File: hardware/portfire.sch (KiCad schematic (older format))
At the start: 32 parts, among them IC4 25AA02E48, IC5 STM32F4xxVxTx, P1 1, P10 10, P11 11, P12 12, P13 13, P14 14, P15 15, P16 16, P17 17, P18 18, P19 19, P2 2, P20 20, P21 21, P22 22, P23 23, P24 24, P25 25, P26 26, P27 27, P28 28, P29 29, P3 3, P30 30, P4 4, P5 5, P6 6, P7 7, P8 8, P9 9

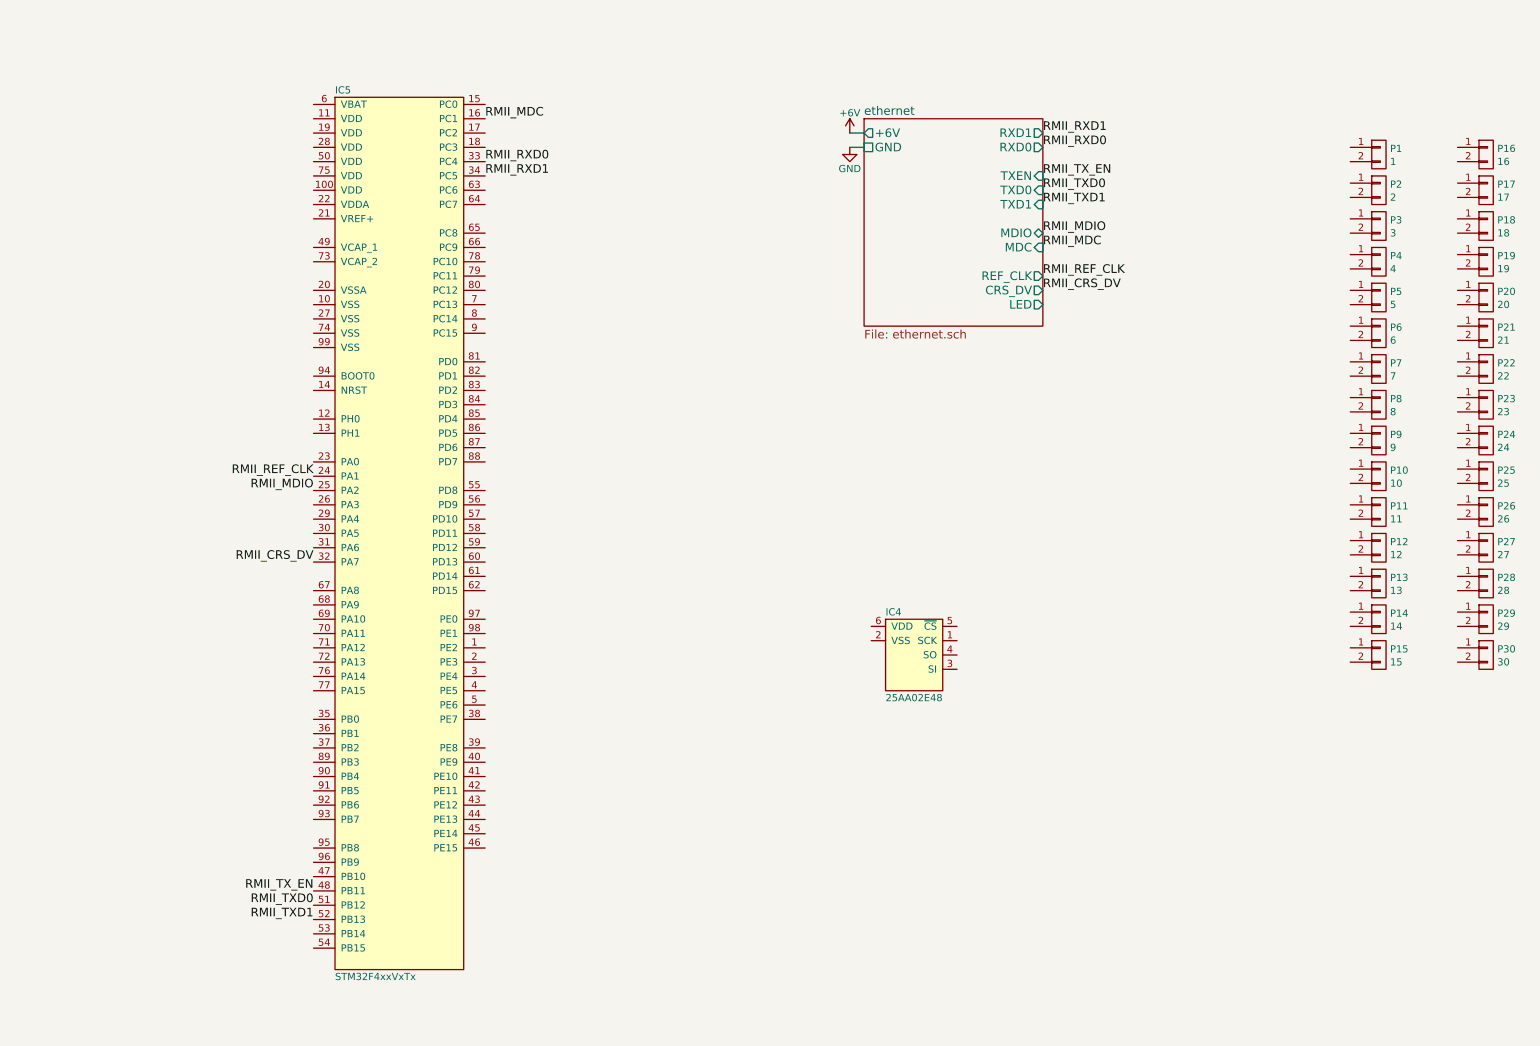
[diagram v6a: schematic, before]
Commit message: Added 3v3 sync buck smps
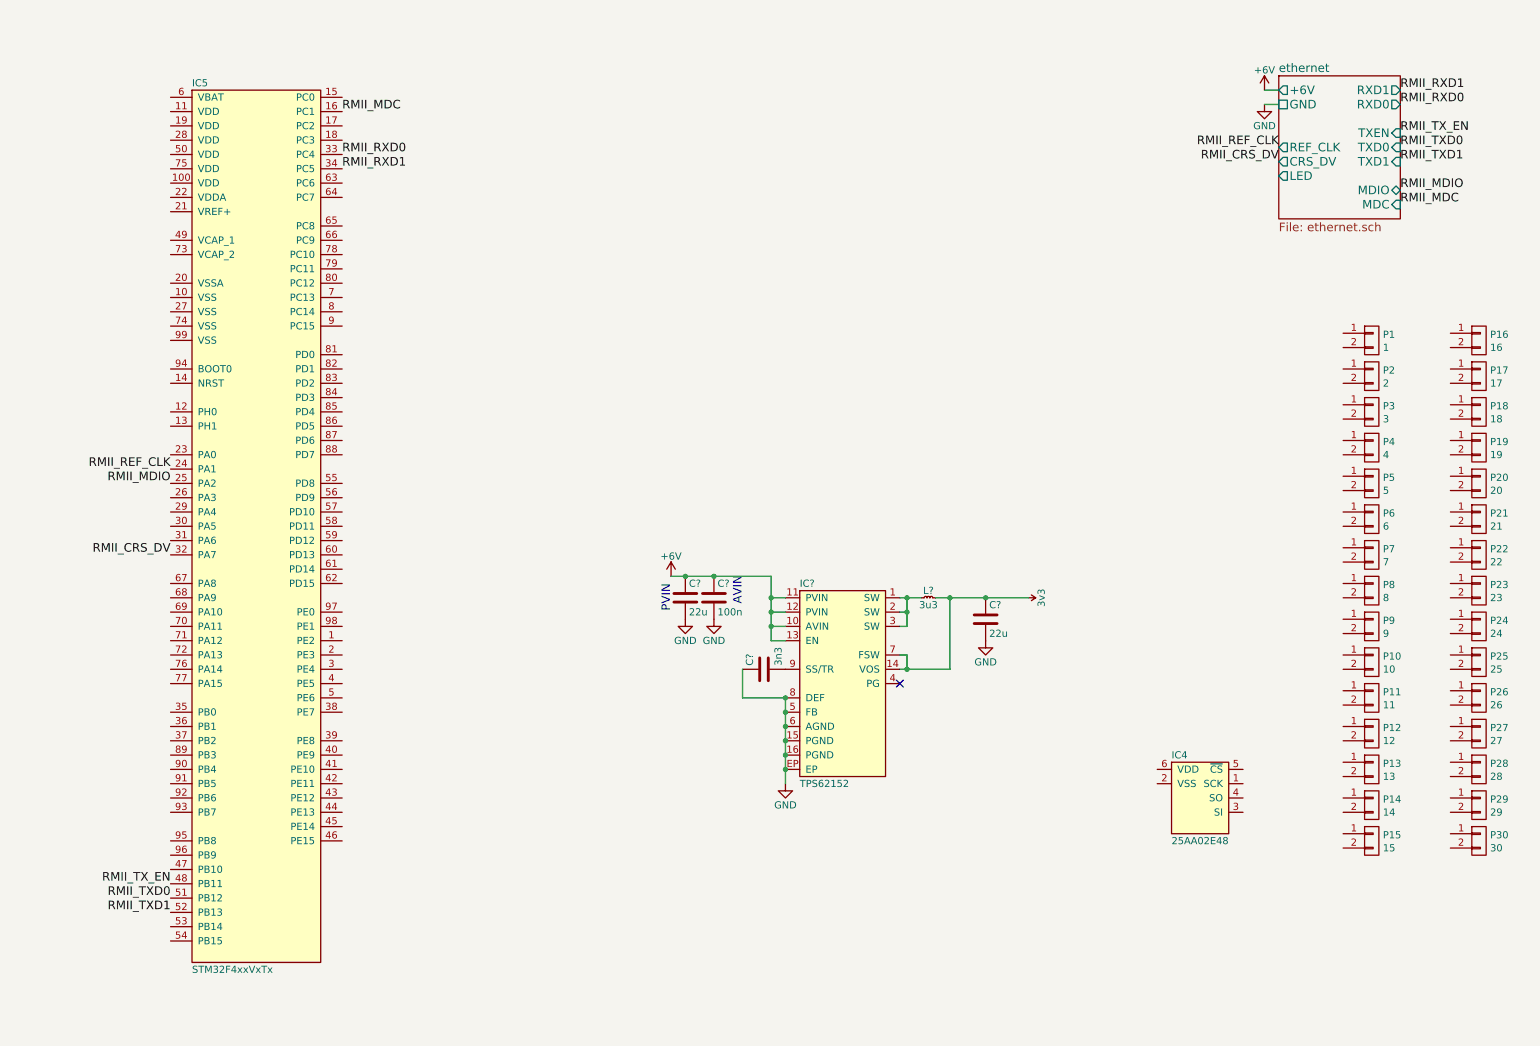
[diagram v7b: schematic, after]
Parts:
- added C? (x2): 22u, agg:1206, symbol C
- added C?: 100n, agg:0603, symbol C
- added C?: 3n3, agg:0603, symbol C
- added IC?: TPS62152, agg:QFN-16-EP-TI, symbol TPS62152
- added L?: 3u3, agg:VLS201610HBX-1, symbol L
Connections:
- net +6V: now also C?.1, C?.1, IC?.10 (AVIN), IC?.11 (PVIN), IC?.12 (PVIN), IC?.13 (EN)
- net GND: now also C?.1, C?.2, C?.2, C?.2, IC?.15 (PGND), IC?.16 (PGND), IC?.5 (FB), IC?.6 (AGND), IC?.8 (DEF), IC?.EP
- new net: IC?.1 (SW), IC?.2 (SW), IC?.3 (SW), L?.1
- new net: C?.2, IC?.9 (SS/TR)
- new net 3v3: C?.1, IC?.14 (VOS), IC?.7 (FSW), L?.2
- no-connect marks 0 -> 1
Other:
- note added: "AVIN"
- note added: "PVIN"
- moved on the sheet: IC4, IC5, P1, P10, P11, P12, P13, P14, P15, P16, P17, P18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

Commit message: stm32 psu and SWD programming
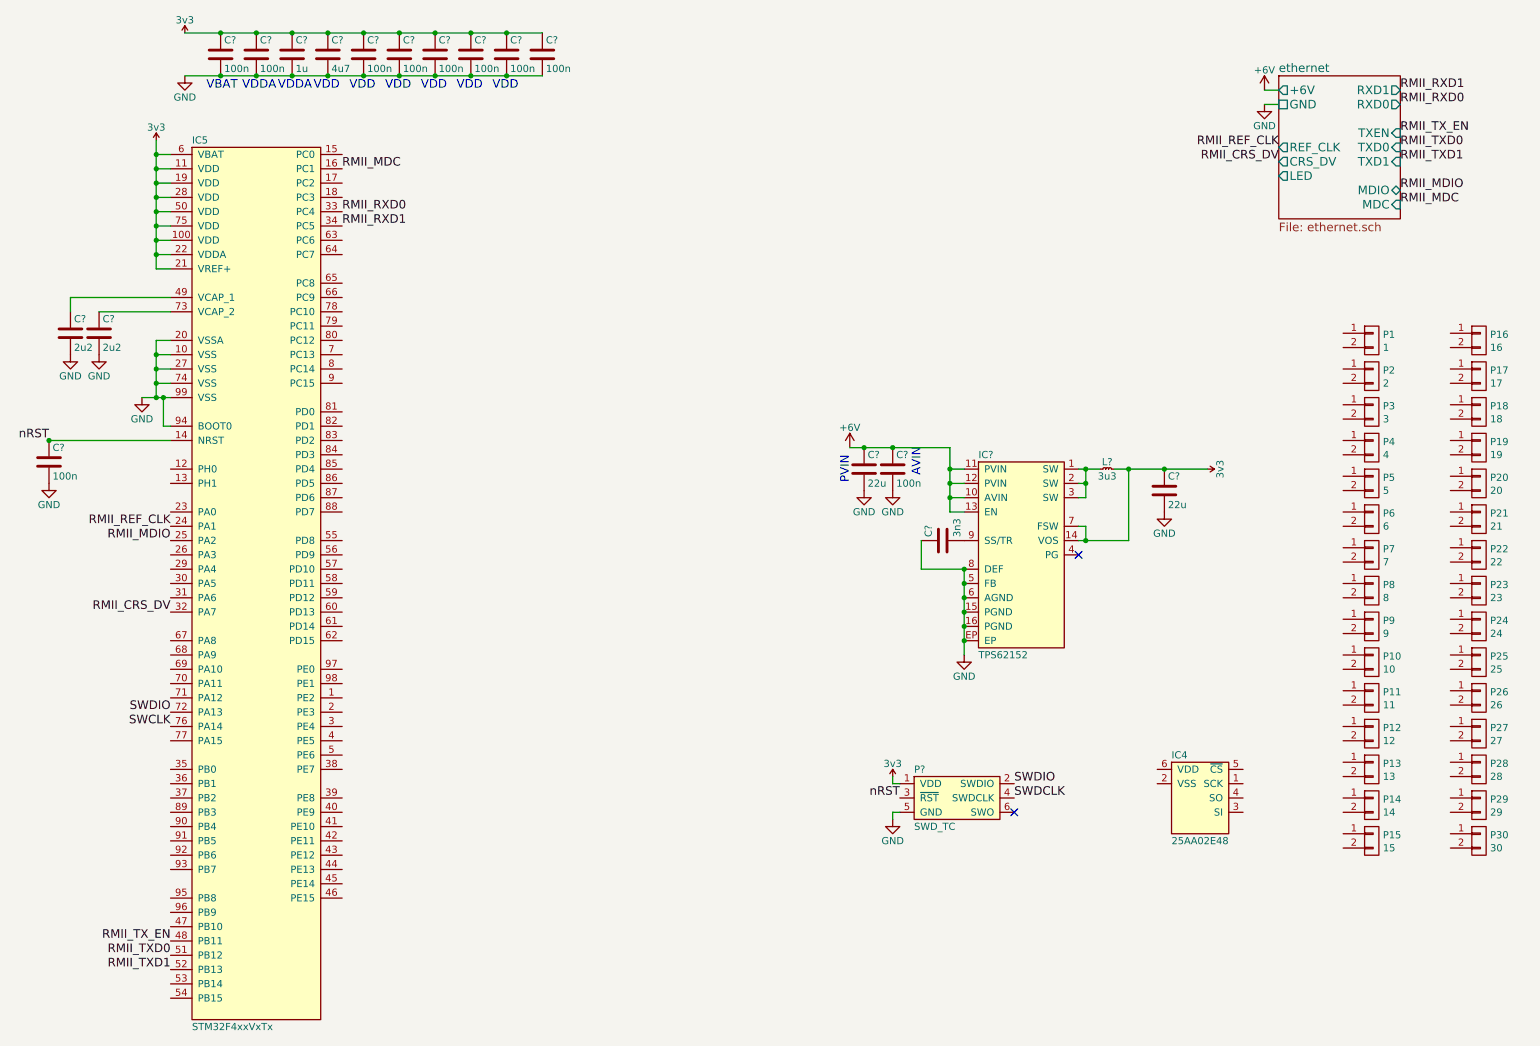
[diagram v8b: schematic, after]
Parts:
- added C? (x9): 100n, agg:0603, symbol C
- added C?: 1u, agg:0603, symbol C
- added C? (x2): 2u2, agg:0603, symbol C
- added C?: 4u7, agg:0603, symbol C
- added P?: SWD_TC, agg:TC2030-NL, symbol SWD_TC
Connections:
- net 3v3: now also IC5.100 (VDD), IC5.11 (VDD), IC5.19 (VDD), IC5.21 (VREF+), IC5.22 (VDDA), IC5.28 (VDD), IC5.50 (VDD), IC5.6 (VBAT), IC5.75 (VDD), C?.1, C?.1, C?.1, C?.1, C?.1, C?.1, C?.1, C?.1, C?.1, C?.1, P?.1 (VDD)
- net GND: now also IC5.10 (VSS), IC5.20 (VSSA), IC5.27 (VSS), IC5.74 (VSS), IC5.94 (BOOT0), IC5.99 (VSS), C?.2, C?.2, C?.2, C?.2, C?.2, C?.2, C?.2, C?.2, C?.2, C?.2, C?.2, C?.2, C?.2, P?.5 (GND)
- net nRST: now reaches IC5.14 (NRST)
- net nRST: now also C?.1, P?.3 (~RST)
- net at IC5.49 (VCAP_1): now also C?.1
- net SWDIO: now reaches IC5.72 (PA13)
- net SWDIO: now also P?.2 (SWDIO)
- net at IC5.73 (VCAP_2): now also C?.1
- net SWCLK: now reaches IC5.76 (PA14)
- new net SWDCLK: P?.4 (SWDCLK)
- no-connect marks 1 -> 2
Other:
- note added: "VBAT"
- note added: "VDD"
- note added: "VDDA"
- moved on the sheet: C?, IC5, IC?, L?
